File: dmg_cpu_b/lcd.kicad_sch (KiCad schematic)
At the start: 75 parts

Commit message: Fixed based on raised issues in PPU region.
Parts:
- added PURE: INVERTER_C, symbol DMG_CPU_Cells:INVERTER_C
- added SONO: INVERTER_A, symbol DMG_CPU_Cells:INVERTER_A
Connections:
- net YCLK: now also PURE.1
- net PPU_1MHz: no longer names the net of RUTU.1 (CLK), SYGU.1 (CLK)
- net PPU_1MHz: now also SONO.2; no longer SAXO.1 (CLK), TALU.2
- net ~{HCLK} renamed ~{YCLK}
- net ~{YCLK}: now also PURE.2
- new net HCLK: SAXO.1 (CLK), SONO.1, TALU.2
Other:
- note added: "YCLK clocks the Vertical counter"
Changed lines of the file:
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@@
   (junction (at 262.89 150.495) (diameter 0) (color 0 0 0 0)
+  )
+  (junction (at 346.075 174.625) (diameter 0) (color 0 0 0 0)
   )
   (no_connect (at 335.915 163.83))
@@
     (stroke (width 0) (type default) (color 0 0 0 0))
   )
+  (wire (pts (xy 347.98 185.42) (xy 346.075 185.42))
+    (stroke (width 0) (type default) (color 0 0 0 0))
+  )
   (wire (pts (xy 168.91 142.875) (xy 171.45 142.875))
     (stroke (width 0) (type default) (color 0 0 0 0))
@@
     (stroke (width 0) (type default) (color 0 0 0 0))
   )
+  (wire (pts (xy 346.075 185.42) (xy 346.075 174.625))
+    (stroke (width 0) (type default) (color 0 0 0 0))
+  )
   (wire (pts (xy 104.775 250.19) (xy 107.315 250.19))
     (stroke (width 0) (type default) (color 0 0 0 0))
@@
     (stroke (width 0) (type default) (color 0 0 0 0))
   )
+  (wire (pts (xy 309.245 158.75) (xy 310.515 158.75))
+    (stroke (width 0) (type default) (color 0 0 0 0))
+  )
   (wire (pts (xy 173.99 189.23) (xy 175.26 189.23))
     (stroke (width 0) (type default) (color 0 0 0 0))
@@
     (stroke (width 0) (type default) (color 0 0 0 0))
   )
-  (wire (pts (xy 338.455 174.625) (xy 348.615 174.625))
+  (wire (pts (xy 338.455 174.625) (xy 346.075 174.625))
     (stroke (width 0) (type default) (color 0 0 0 0))
   )
@@
     (stroke (width 0) (type default) (color 0 0 0 0))
   )
-  (wire (pts (xy 107.95 71.12) (xy 106.68 71.12))
+  (wire (pts (xy 107.95 71.12) (xy 102.235 71.12))
     (stroke (width 0) (type default) (color 0 0 0 0))
   )
@@
     (stroke (width 0) (type default) (color 0 0 0 0))
   )
-  (wire (pts (xy 299.085 158.75) (xy 310.515 158.75))
+  (wire (pts (xy 286.385 158.75) (xy 296.545 158.75))
     (stroke (width 0) (type default) (color 0 0 0 0))
   )
@@
     (stroke (width 0) (type default) (color 0 0 0 0))
   )
+  (wire (pts (xy 360.68 185.42) (xy 370.205 185.42))
+    (stroke (width 0) (type default) (color 0 0 0 0))
+  )
   (wire (pts (xy 78.105 103.505) (xy 78.105 99.06))
     (stroke (width 0) (type default) (color 0 0 0 0))
@@
     (stroke (width 0) (type default) (color 0 0 0 0))
   )
+  (wire (pts (xy 346.075 174.625) (xy 370.205 174.625))
+    (stroke (width 0) (type default) (color 0 0 0 0))
+  )
   (wire (pts (xy 295.275 240.03) (xy 296.545 240.03))
     (stroke (width 0) (type default) (color 0 0 0 0))
@@
     (stroke (width 0) (type default) (color 0 0 0 0))
   )
-  (wire (pts (xy 294.005 149.86) (xy 294.005 163.83))
+  (wire (pts (xy 283.21 149.86) (xy 283.21 163.83))
     (stroke (width 0) (type default) (color 0 0 0 0))
   )
@@
     (stroke (width 0) (type default) (color 0 0 0 0))
   )
-  (wire (pts (xy 294.005 163.83) (xy 315.595 163.83))
+  (wire (pts (xy 283.21 163.83) (xy 315.595 163.83))
     (stroke (width 0) (type default) (color 0 0 0 0))
   )
@@
     (stroke (width 0) (type default) (color 0 0 0 0))
   )
-  (wire (pts (xy 361.95 149.86) (xy 294.005 149.86))
+  (wire (pts (xy 361.95 149.86) (xy 283.21 149.86))
     (stroke (width 0) (type default) (color 0 0 0 0))
   )
@@
   (bus (pts (xy 273.685 128.27) (xy 273.685 108.585))
     (stroke (width 0) (type default) (color 0 0 0 0))
+  )
+  (text "YCLK clocks the Vertical counter" (at 373.38 179.705 0)
+    (effects (font (size 1.27 1.27)) (justify left bottom))
   )
   (text "Move VENA and TALU to page 29 later" (at 171.45 131.445 0)
@@
     (effects (font (size 1.27 1.27)) (justify right bottom))
   )
+  (label "~{YCLK}" (at 370.205 185.42 180)
+    (effects (font (size 1.27 1.27)) (justify right bottom))
+  )
   (label "LCD_X2" (at 313.055 100.965 0)
     (effects (font (size 1.27 1.27)) (justify left bottom))
@@
     (effects (font (size 1.27 1.27)) (justify right bottom))
   )
+  (label "~{YCLK}" (at 102.235 71.12 0)
+    (effects (font (size 1.27 1.27)) (justify left bottom))
+  )
   (label "LCD_X6" (at 313.055 130.175 0)
     (effects (font (size 1.27 1.27)) (justify left bottom))
   )
-  (label "PPU_1MHz" (at 213.995 145.415 0)
+  (label "HCLK" (at 213.995 145.415 0)
     (effects (font (size 1.27 1.27)) (justify left bottom))
   )
@@
     (effects (font (size 1.27 1.27)) (justify left bottom))
   )
-  (label "YCLK" (at 348.615 174.625 180)
+  (label "YCLK" (at 370.205 174.625 180)
     (effects (font (size 1.27 1.27)) (justify right bottom))
   )
@@
     (effects (font (size 1.27 1.27)) (justify left bottom))
   )
-  (label "PPU_1MHz" (at 299.085 158.75 0)
+  (label "HCLK" (at 286.385 158.75 0)
     (effects (font (size 1.27 1.27)) (justify left bottom))
   )
@@
     (effects (font (size 1.27 1.27)) (justify right))
   )
-  (hierarchical_label "~{HCLK}" (shape input) (at 106.68 71.12 180)
-    (effects (font (size 1.27 1.27)) (justify right))
+  (hierarchical_label "~{YCLK}" (shape output) (at 370.205 185.42 0)
+    (effects (font (size 1.27 1.27)) (justify left))
   )
   (hierarchical_label "FF40_D[0..7]" (shape input) (at 106.045 55.88 180)
@@
     (effects (font (size 1.27 1.27)) (justify right))
   )
-  (hierarchical_label "PPU_1MHz" (shape output) (at 214.63 139.7 0)
+  (hierarchical_label "HCLK" (shape output) (at 214.63 139.7 0)
     (effects (font (size 1.27 1.27)) (justify left))
   )
@@
     (effects (font (size 1.27 1.27)) (justify right))
   )
-  (hierarchical_label "YCLK" (shape output) (at 348.615 174.625 0)
+  (hierarchical_label "YCLK" (shape output) (at 370.205 174.625 0)
     (effects (font (size 1.27 1.27)) (justify left))
   )
@@
     )
     (property "Datasheet" "http://iceboy.a-singer.de/doc/dmg_cells.html#inv_c" (id 3) (at 179.07 99.06 0)
+      (effects (font (size 1.27 1.27)) hide)
+    )
+    (pin "1")
+    (pin "2")
+  )
+  (symbol (lib_id "DMG_CPU_Cells:INVERTER_C") (at 354.33 185.42 0) (unit 1)
+    (in_bom yes) (on_board yes) (fields_autoplaced)
+    (property "Reference" "PURE" (id 0) (at 354.33 177.9102 0))
+    (property "Value" "INVERTER_C" (id 1) (at 354.33 180.4471 0))
+    (property "Footprint" "" (id 2) (at 351.79 185.42 0)
+      (effects (font (size 1.27 1.27)) hide)
+    )
+    (property "Datasheet" "http://iceboy.a-singer.de/doc/dmg_cells.html#inv_c" (id 3) (at 355.6 193.04 0)
       (effects (font (size 1.27 1.27)) hide)
     )
@@
     (pin "3")
   )
+  (symbol (lib_id "DMG_CPU_Cells:INVERTER_A") (at 302.895 158.75 0) (unit 1)
+    (in_bom yes) (on_board yes) (fields_autoplaced)
+    (property "Reference" "SONO" (id 0) (at 302.895 151.2402 0))
+    (property "Value" "INVERTER_A" (id 1) (at 302.895 153.7771 0))
+    (property "Footprint" "" (id 2) (at 300.355 158.75 0)
+      (effects (font (size 1.27 1.27)) hide)
+    )
+    (property "Datasheet" "http://iceboy.a-singer.de/doc/dmg_cells.html#inv_a" (id 3) (at 304.165 166.37 0)
+      (effects (font (size 1.27 1.27)) hide)
+    )
+    (pin "1")
+    (pin "2")
+  )
   (symbol (lib_id "DMG_CPU_Cells:INVERTER_A") (at 282.575 66.675 0) (unit 1)

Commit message: Fixes and and rearranged schematics whereever possible to improve legibility.
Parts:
- POKY: value OR_2 -> NOR_LATCH; symbol DMG_CPU_Cells:OR_2 -> DMG_CPU_Cells:NOR_LATCH
- SACU: value NOR_2 -> OR_2; symbol DMG_CPU_Cells:NOR_2 -> DMG_CPU_Cells:OR_2
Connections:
- net ~{MODE3}: now also POKY.4 (RESET); no longer POKY.2
- net NYKA: no longer names the net of NYKA.6 (Q), PORY.3 (D), SUVU.3
- no-connect marks 10 -> 11
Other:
- moved on the sheet: CP, LOBY, MEDA, MURE, NAFY, NERU, NYKA, PAHO, POFY, POME, PORY, PYGO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

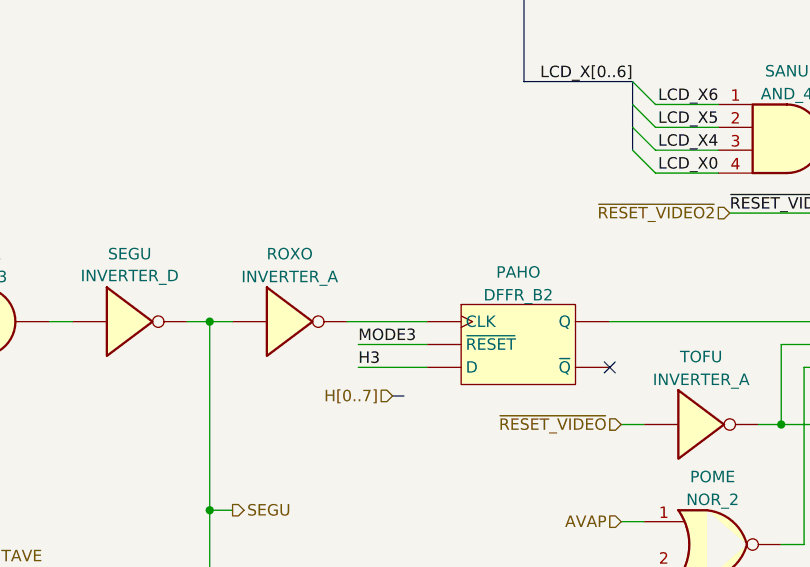
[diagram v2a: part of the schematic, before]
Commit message: BG and WIN sheets added.
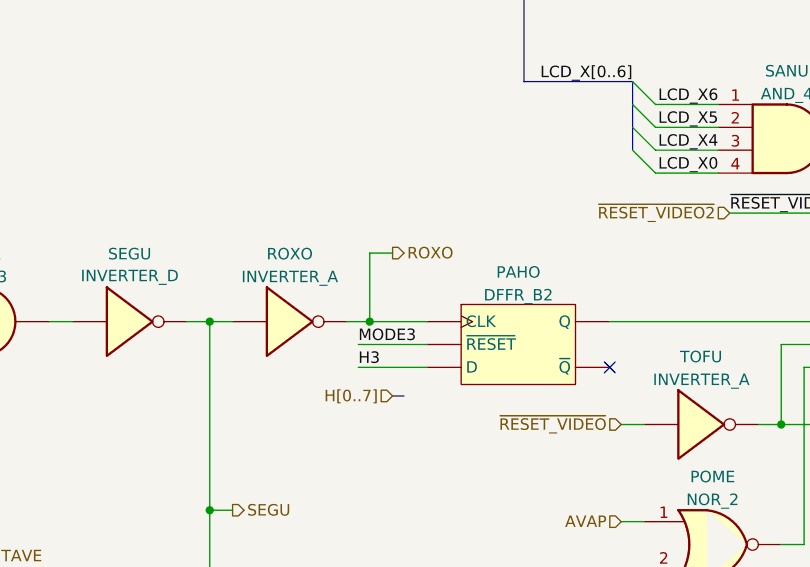
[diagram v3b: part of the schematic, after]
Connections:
- net ROXO: now reaches PAHO.1 (CLK), ROXO.2
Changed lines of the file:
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@@
   (junction (at 75.565 191.77) (diameter 0) (color 0 0 0 0)
+  )
+  (junction (at 256.54 200.025) (diameter 0) (color 0 0 0 0)
   )
   (junction (at 310.515 158.75) (diameter 0) (color 0 0 0 0)
@@
     (stroke (width 0) (type default) (color 0 0 0 0))
   )
-  (wire (pts (xy 262.89 200.025) (xy 254 200.025))
-    (stroke (width 0) (type default) (color 0 0 0 0))
-  )
   (wire (pts (xy 271.145 46.99) (xy 276.225 46.99))
     (stroke (width 0) (type default) (color 0 0 0 0))
@@
     (stroke (width 0) (type default) (color 0 0 0 0))
   )
+  (wire (pts (xy 256.54 200.025) (xy 254 200.025))
+    (stroke (width 0) (type default) (color 0 0 0 0))
+  )
   (wire (pts (xy 335.915 174.625) (xy 338.455 174.625))
     (stroke (width 0) (type default) (color 0 0 0 0))
@@
     (stroke (width 0) (type default) (color 0 0 0 0))
   )
+  (wire (pts (xy 256.54 200.025) (xy 262.89 200.025))
+    (stroke (width 0) (type default) (color 0 0 0 0))
+  )
   (wire (pts (xy 78.105 99.06) (xy 75.565 99.06))
     (stroke (width 0) (type default) (color 0 0 0 0))
@@
     (stroke (width 0) (type default) (color 0 0 0 0))
   )
+  (wire (pts (xy 256.54 192.405) (xy 259.08 192.405))
+    (stroke (width 0) (type default) (color 0 0 0 0))
+  )
   (wire (pts (xy 204.47 189.865) (xy 204.47 197.485))
     (stroke (width 0) (type default) (color 0 0 0 0))
   )
   (wire (pts (xy 87.63 93.98) (xy 88.9 93.98))
+    (stroke (width 0) (type default) (color 0 0 0 0))
+  )
+  (wire (pts (xy 256.54 200.025) (xy 256.54 192.405))
     (stroke (width 0) (type default) (color 0 0 0 0))
   )
@@
     (effects (font (size 1.27 1.27)) (justify right))
   )
+  (hierarchical_label "ROXO" (shape output) (at 259.08 192.405 0)
+    (effects (font (size 1.27 1.27)) (justify left))
+  )
   (hierarchical_label "SEGU" (shape output) (at 241.3 220.98 0)

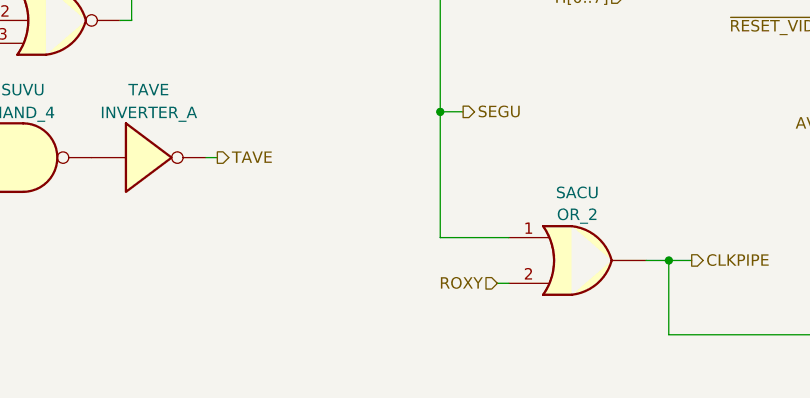
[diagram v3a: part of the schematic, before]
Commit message: VRAM interface sheet added but various edits in existing sheets. Notable merge of RESET, CLOCKS and FF04 DIV sheets
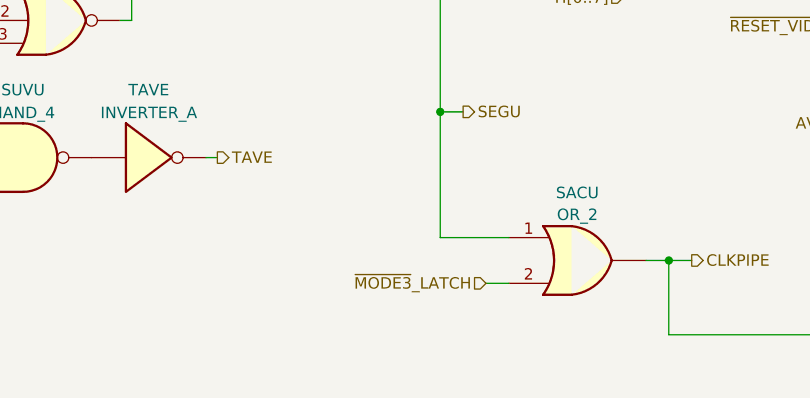
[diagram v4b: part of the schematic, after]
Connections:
- net ROXY renamed ~{MODE3}_LATCH
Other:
- company: (none) -> CC-BY-SA-4.0 Régis Galland & Michael Singer -- Derived work from Furrtek
- title: (none) -> DMG CPU B
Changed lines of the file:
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@@
 (kicad_sch (version 20211123) (generator eeschema)
   (paper "A3")
+  (title_block
+    (title "DMG CPU B")
+    (date "2022-05-02")
+    (rev "0")
+    (company "CC-BY-SA-4.0 Régis Galland & Michael Singer -- Derived work from Furrtek")
+    (comment 1 "https://github.com/msinger/dmg-schematics")
+  )
   (junction (at 299.085 86.36) (diameter 0) (color 0 0 0 0)
   )
@@
     (stroke (width 0) (type default) (color 0 0 0 0))
   )
-  (wire (pts (xy 245.11 240.03) (xy 246.38 240.03))
-    (stroke (width 0) (type default) (color 0 0 0 0))
-  )
   (wire (pts (xy 78.105 99.06) (xy 88.9 99.06))
     (stroke (width 0) (type default) (color 0 0 0 0))
@@
   )
   (wire (pts (xy 78.105 194.31) (xy 83.185 194.31))
+    (stroke (width 0) (type default) (color 0 0 0 0))
+  )
+  (wire (pts (xy 246.38 240.03) (xy 243.84 240.03))
     (stroke (width 0) (type default) (color 0 0 0 0))
   )
@@
     (effects (font (size 1.27 1.27)) (justify right))
   )
+  (hierarchical_label "~{MODE3}_LATCH" (shape input) (at 243.84 240.03 180)
+    (effects (font (size 1.27 1.27)) (justify right))
+  )
   (hierarchical_label "PX9" (shape input) (at 307.975 240.665 180)
     (effects (font (size 1.27 1.27)) (justify right))
@@
     (effects (font (size 1.27 1.27)) (justify right))
   )
-  (hierarchical_label "ROXY" (shape input) (at 245.11 240.03 180)
-    (effects (font (size 1.27 1.27)) (justify right))
-  )

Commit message: sprite y comparator added
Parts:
- added LAMA, WOJO: NOR_2, symbol DMG_CPU_Cells:NOR_2
- added LAXE, LUSU, LYRY, MYMA, MYVO, NAKO, NENY, NOFU, PARU, XOTA, XUHA, XYFY, XYSO, XYVA: INVERTER_A, symbol DMG_CPU_Cells:INVERTER_A
- added LAXU, LOVY, LYZU, MESU, MYTA, NAPO, NYPE, NYVA, POPU, WOSU, WUVU: DFFR_B2, symbol DMG_CPU_Cells:DFFR_B2
- added LEBO, NOGU: NAND_2, symbol DMG_CPU_Cells:NAND_2
- added LENA, XOCE, XUPY: INVERTER_B, symbol DMG_CPU_Cells:INVERTER_B
- added LONY: NAND_LATCH, symbol DMG_CPU_Cells:NAND_LATCH
- added LURY, MOFU, NETA, POTU, XYVO: AND_2, symbol DMG_CPU_Cells:AND_2
- added MOCE, NYDY: NAND_3, symbol DMG_CPU_Cells:NAND_3
- added MYSO: NOR_3, symbol DMG_CPU_Cells:NOR_3
- added NOKO: AND_4, symbol DMG_CPU_Cells:AND_4
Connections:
- net CLK2: now also LEBO.1, LYZU.1 (CLK), MYVO.1
- net HCLK: now also NYPE.1 (CLK)
- net LYRY: now also LOVY.3 (D), LYRY.2
- net MODE3: now also LURY.2, LYZU.2 (~{RESET}), LYZU.4 (~{RESET})
- net RESET_VIDEO3: now also LAMA.2
- net V0: now also NOKO.4
- net V3: now also NOKO.3
- net V4: now also NOKO.2, XYVO.1
- net V7: now also NOKO.1, XYVO.2
- net ~{CLK2}: now also LOVY.1 (CLK), MYVO.2
- net ~{MODE3}: now also MYSO.1
- net ~{RESET_VIDEO2}: now also MYTA.2 (~{RESET}), MYTA.4 (~{RESET}), NAPO.2 (~{RESET}), NAPO.4 (~{RESET}), NYPE.2 (~{RESET}), NYPE.4 (~{RESET}), POPU.2 (~{RESET}), POPU.4 (~{RESET})
- net ~{RESET_VIDEO}: now also WOSU.2 (~{RESET}), WOSU.4 (~{RESET}), WUVU.2 (~{RESET}), WUVU.4 (~{RESET})
- net FEPO renamed SPRITE_X_MATCH
- net NAPO: no longer names the net of MAGU.2 (1)
- net NAPO: now also NAPO.6 (Q)
- net WUVU_~{Q}: no longer names the net of VENA.1 (CLK)
- net WUVU_~{Q}: now also WOJO.2, WOSU.3 (D), WUVU.3 (D), WUVU.5 (~{Q}), XUPY.1
- net YCLK renamed VCLK
- net VCLK: now also NYPE.3 (D)
- net ~{YCLK_REG}: no longer names the net of MEDA.1 (CLK)
- net ~{YCLK_REG}: now also MYTA.1 (CLK), NYPE.5 (~{Q})
- net ~{YCLK} renamed ~{VCLK}
- new net: MESU.3 (D), MESU.5 (~{Q}), NYVA.1 (CLK)
- new net: NYVA.3 (D), NYVA.5 (~{Q})
- new net: MOCE.1, NOFU.1, NYVA.6 (Q)
- new net: NENY.2, POTU.1
- new net: MESU.6 (Q), NAKO.1, NYDY.2
- new net: MOFU.1, NAKO.2, NOGU.1
- new net: LAXE.1, LAXU.6 (Q), LYZU.3 (D), MOCE.3
- new net: LAXE.2, MYSO.2
- new net: LONY.1 (~{RESET}), LURY.3
- new net: LONY.3 (Q), LUSU.1, MYMA.1
- new net: LEBO.2, LYRY.1, MOCE.4
- new net: NYPE.6 (Q), POPU.1 (CLK)
- new net: POPU.3 (D), XYVO.3
- new net: PARU.1, POPU.5 (~{Q})
- new net: NAPO.1 (CLK), POPU.6 (Q)
- new net: NOFU.2, NOGU.2, NYDY.3, XUHA.1
- new net: NENY.1, NETA.1, NOGU.3
- new net: XOTA.1, XYVA.2
- new net: WUVU.1 (CLK), XOTA.2, XYFY.1
- new net: MYTA.3 (D), NOKO.5
- new net: LAMA.1, MYTA.6 (Q)
- new net: MOFU.2, MYSO.4, NYDY.1
- new net: LYZU.6 (Q), MYSO.3
- new net: LAXU.3 (D), LAXU.5 (~{Q}), MESU.1 (CLK)
- new net: WOSU.1 (CLK), XYFY.2
- new net: LAXU.1 (CLK), LEBO.3
- new net: LENA.1, LUSU.2
- new net: NAPO.3 (D), NAPO.5 (~{Q})
- new net: WOJO.3, XYSO.1
- new net: LOVY.5 (~{Q}), LURY.1
- new net: WOSU.6 (Q), XOCE.1
- new net: WOJO.1, WOSU.5 (~{Q})
- new net CLK1: XYVA.1
- new net INT_VBL: PARU.2
- new net LENA: LENA.2, NETA.2, POTU.2
- new net MOFU: MOFU.3
- new net MYMA: MYMA.2
- new net NETA: NETA.3
- new net NYDY: NYDY.4
- new net NYXU: LAXU.2 (~{RESET}), LAXU.4 (~{RESET}), LONY.4 (~{SET}), LOVY.2 (~{RESET}), LOVY.4 (~{RESET}), MESU.2 (~{RESET}), MESU.4 (~{RESET}), MOCE.2, NYVA.2 (~{RESET}), NYVA.4 (~{RESET})
- new net POTU: POTU.3
- new net XOCE: XOCE.2
- new net XUHA: XUHA.2
- new net XUPY: XUPY.2
- new net XYSO: XYSO.2
- new net ~{V_RESET}: LAMA.3
- no-connect marks 11 -> 16
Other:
- note added: "INT = '1' when V >= 144"
- note added: "In https://wavedrom.com/editor.html {signal: [ {name: 'CLK1', wave: '01010101010101010101010101|0101010101010101010101010101010'}, {name: 'RESET_VIDEO', wave: '1.0.......................|...............................'}, {name: 'WUVU./Q', wave: '1..0.1.0.1.0.1.0.1.0.1.0.1|.0.1.0.1.0.1.0.1.0.1.0.1.0.1.0.'}, {name: 'XUPY', wave: '0..1.0.1.0.1.0.1.0.1.0.1.0|.1.0.1.0.1.0.1.0.1.0.1.0.1.0.1.'}, {name: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"
- note added: "VCLK clocks the Vertical counter"
- note added: "~{V_RESET} = '0' when V = 153 and VCLK falling edge"
- note removed: "Move VENA and TALU to page 29 later"
- note removed: "YCLK clocks the Vertical counter"
- moved on the sheet: CP, CPG, CPL, FR, KAHE, KASA, KEBO, KEDY, KOFO, KUPA, KYMO, LEBE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
